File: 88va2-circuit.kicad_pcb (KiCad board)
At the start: 2 copper layers, 380 x 237.5 mm, 31 parts, among them CN2 FDD, CN4 TEXT BUS, CN5 LED, IC20 7407, IC21 uPD4990AC, IC22 DIP-14_W7.62mm, IC65 D65101GD110, X2 32.768K

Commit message: add internal layers (GND and power)
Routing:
- net GND: track 139.7 -> 1252.1 mm, vias 4 -> 10
- net +5V: track 5.94 -> 735.6 mm
- net (no net): track 1731.3 -> 1751.0 mm
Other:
- copper layers 2 -> 4

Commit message: fix IC65
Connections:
- IC65 pad 1: unconnected-(IC65-VDD-Pad1) -> +5V
- IC65 pad 40: unconnected-(IC65-VDD-Pad40) -> +5V
- IC65 pad 74: unconnected-(IC65-CLC2-Pad74) -> C2
- IC65 pad 75: unconnected-(IC65-CLC1-Pad75) -> C1
- IC65 pad 76: unconnected-(IC65-CLC0-Pad76) -> C0
- IC65 pad 77: unconnected-(IC65-CLSTB-Pad77) -> CSTB
- IC65 pad 78: unconnected-(IC65-CLDO-Pad78) -> CDO
- IC65 pad 82: unconnected-(IC65-CLCLK-Pad82) -> CCLK
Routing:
- net +5V: track 735.6 -> 826.3 mm, vias 0 -> 2

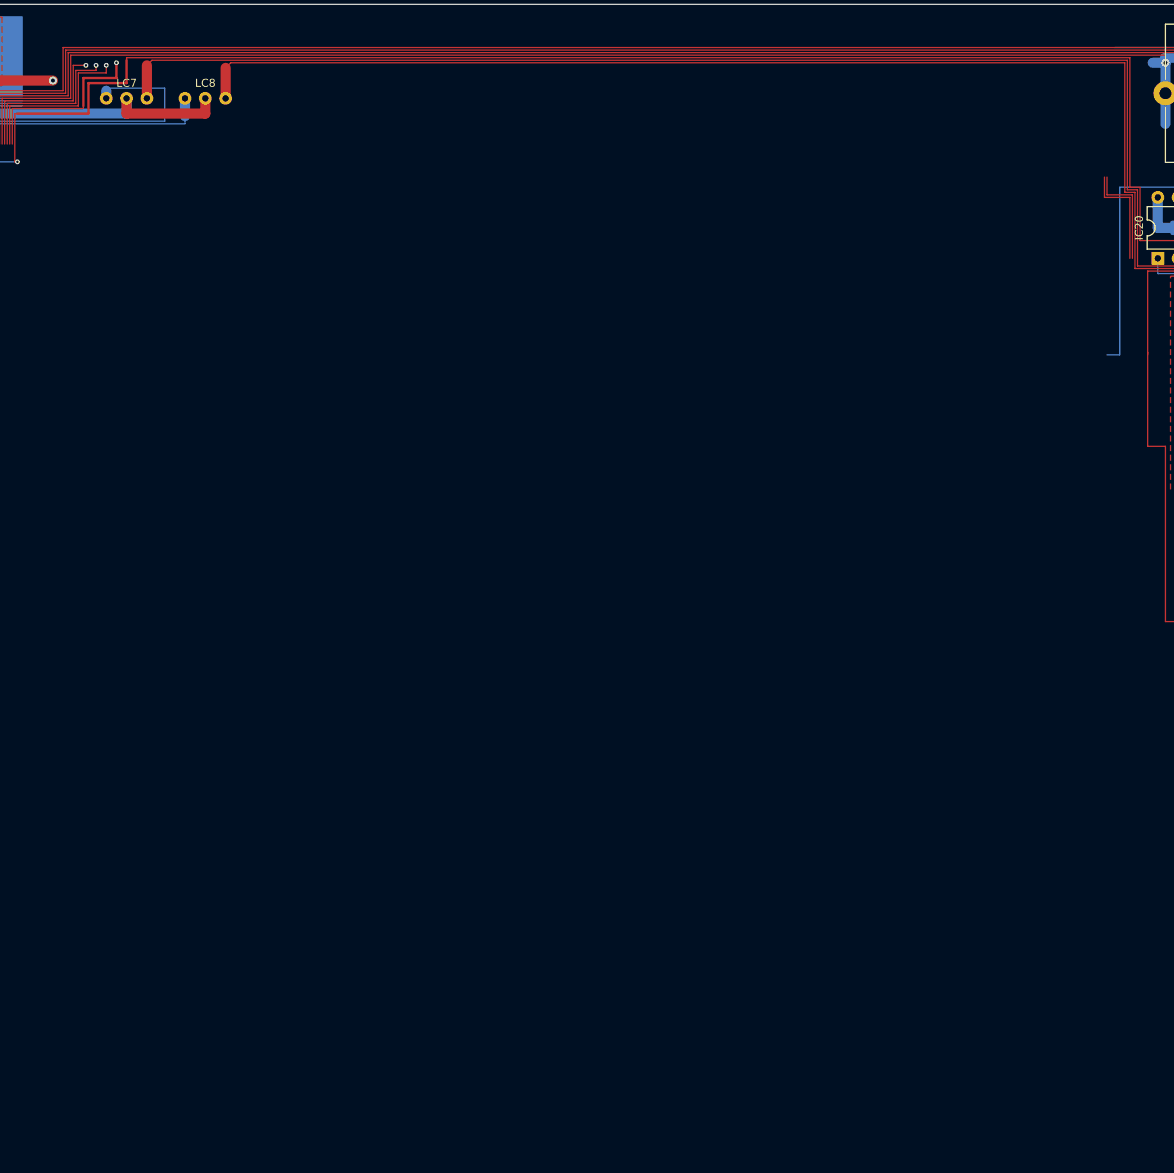
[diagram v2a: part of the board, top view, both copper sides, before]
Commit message: add IC13, MR6, IC9, IC1 footprints
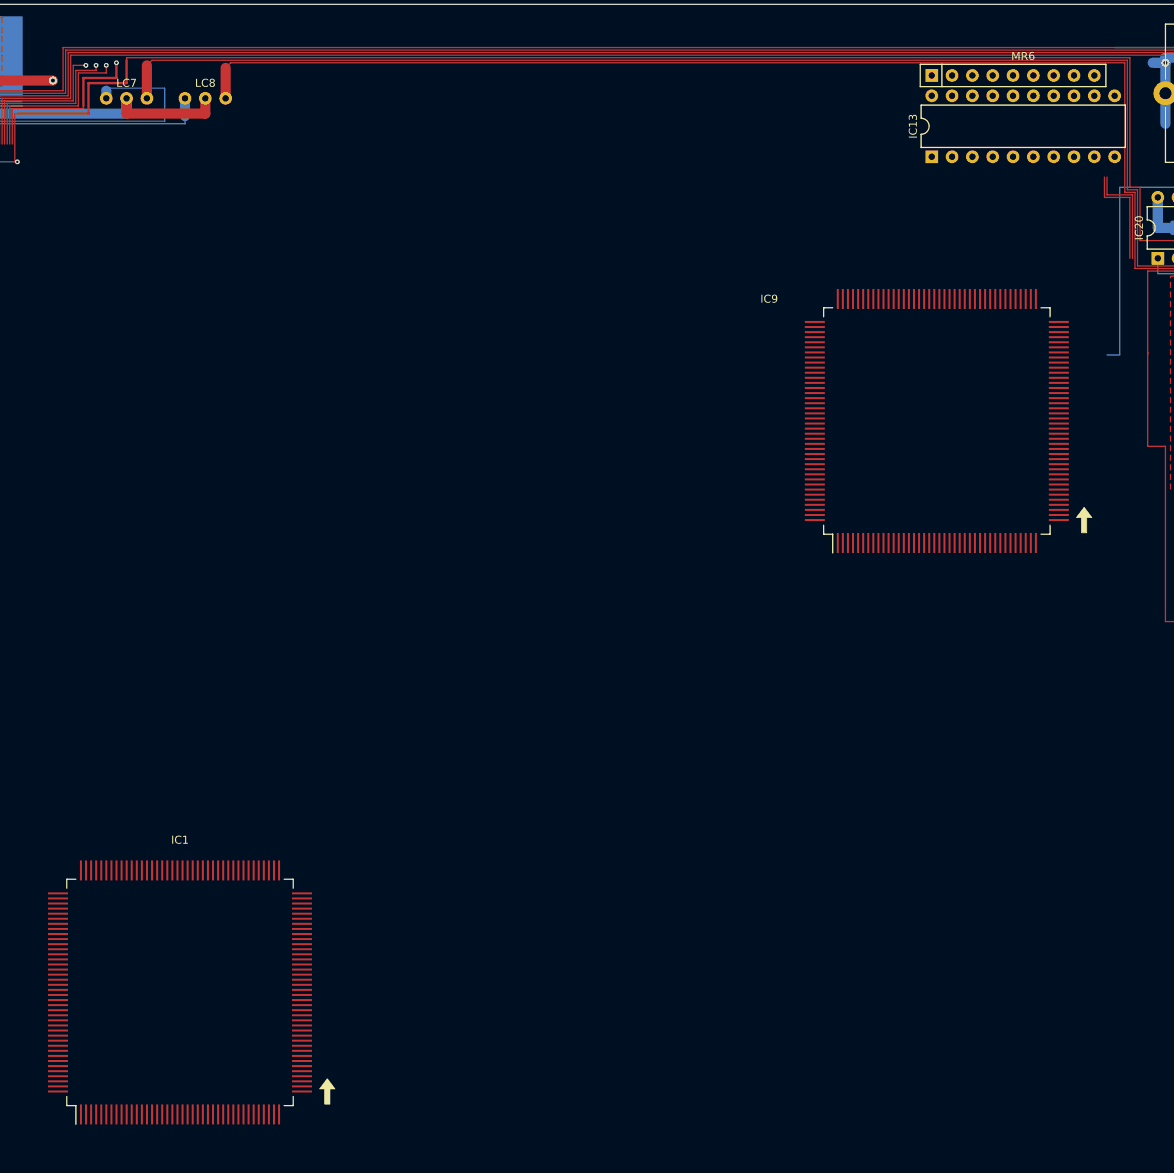
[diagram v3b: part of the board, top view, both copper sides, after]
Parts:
- added IC1: D65101GD055, 88va_Library:QFP-160_28x28_Pitch0.635mm, F.Cu at (45.4, 140.0)
- added IC13: SN74ALS374N, Package_DIP:DIP-20_W7.62mm, F.Cu at (139.3, 35.5)
- added IC9: D65200GD076, 88va_Library:QFP-160_28x28_Pitch0.635mm, F.Cu at (140.0, 68.6)
- added MR6: 33kΩ, Resistor_THT:R_Array_SIP9, F.Cu at (139.3, 25.4)

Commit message: wire IC13
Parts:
- added C60: C_Small, Capacitor_SMD:C_1206_3216Metric, B.Cu at (158.2, 31.7)
- moved IC9 0.46 mm to (139.6, 68.3)
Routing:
- net (no net): track 1751.0 -> 2510.1 mm, vias 29 -> 58
- net GCS0: track 0.00 -> 84.8 mm, vias 0 -> 2
- net Net-(IC13-7D): track 0.00 -> 70.5 mm, vias 0 -> 1
- net Net-(IC13-2D): track 0.00 -> 68.9 mm, vias 0 -> 2
- net Net-(IC13-6D): track 0.00 -> 65.1 mm, vias 0 -> 1
- net Net-(IC13-1D): track 0.00 -> 63.8 mm
- net Net-(IC13-5D): track 0.00 -> 55.9 mm
- net GCS1: track 0.00 -> 54.9 mm, vias 0 -> 1
- net Net-(IC13-3D): track 0.00 -> 54.9 mm
- net Net-(IC13-4D): track 0.00 -> 53.7 mm
- net Net-(IC13-CLK): track 0.00 -> 36.2 mm
- net +5V: track 826.3 -> 862.1 mm, vias 2 -> 4
- net Net-(IC13-8D): track 0.00 -> 12.1 mm
- net GND: track 1252.1 -> 1258.4 mm
- net GCS2: track 0.00 -> 2.54 mm

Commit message: wire IC13
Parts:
- added R18: ??, Resistor_SMD:R_1206_3216Metric, B.Cu at (96.3, 24.1)
- added REF**: DIP-20_W7.62mm, Package_DIP:DIP-20_W7.62mm, F.Cu at (111.4, 35.5)
- moved LC6 0.95 mm to (20.3, 40.6)
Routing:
- net ILCLK1: track 0.00 -> 323.8 mm, vias 0 -> 2
- net GCS2: track 2.54 -> 313.0 mm, vias 0 -> 1
- net GCS3: track 0.00 -> 304.8 mm, vias 0 -> 2
- net ILCLK0: track 0.00 -> 303.8 mm, vias 0 -> 2
- net GCS1: track 54.9 -> 345.1 mm, vias 1 -> 3
- net DTM0: track 0.00 -> 285.7 mm, vias 0 -> 2
- net GCS0: track 84.8 -> 356.5 mm, vias 2 -> 3
- net Net-(IC13-OE): track 0.00 -> 96.4 mm, vias 0 -> 3
- net (no net): track 2510.1 -> 2450.4 mm, vias 58 -> 60
- net Net-(IC13-8D): track 12.1 -> 54.2 mm
- net Net-(IC13-5D): track 55.9 -> 67.0 mm
- net +5V: track 862.1 -> 853.6 mm, vias 4 -> 3
- net Net-(IC13-6D): track 65.1 -> 72.1 mm
- net Net-(IC13-3D): track 54.9 -> 61.3 mm
- net Net-(IC13-7D): track 70.5 -> 76.5 mm
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
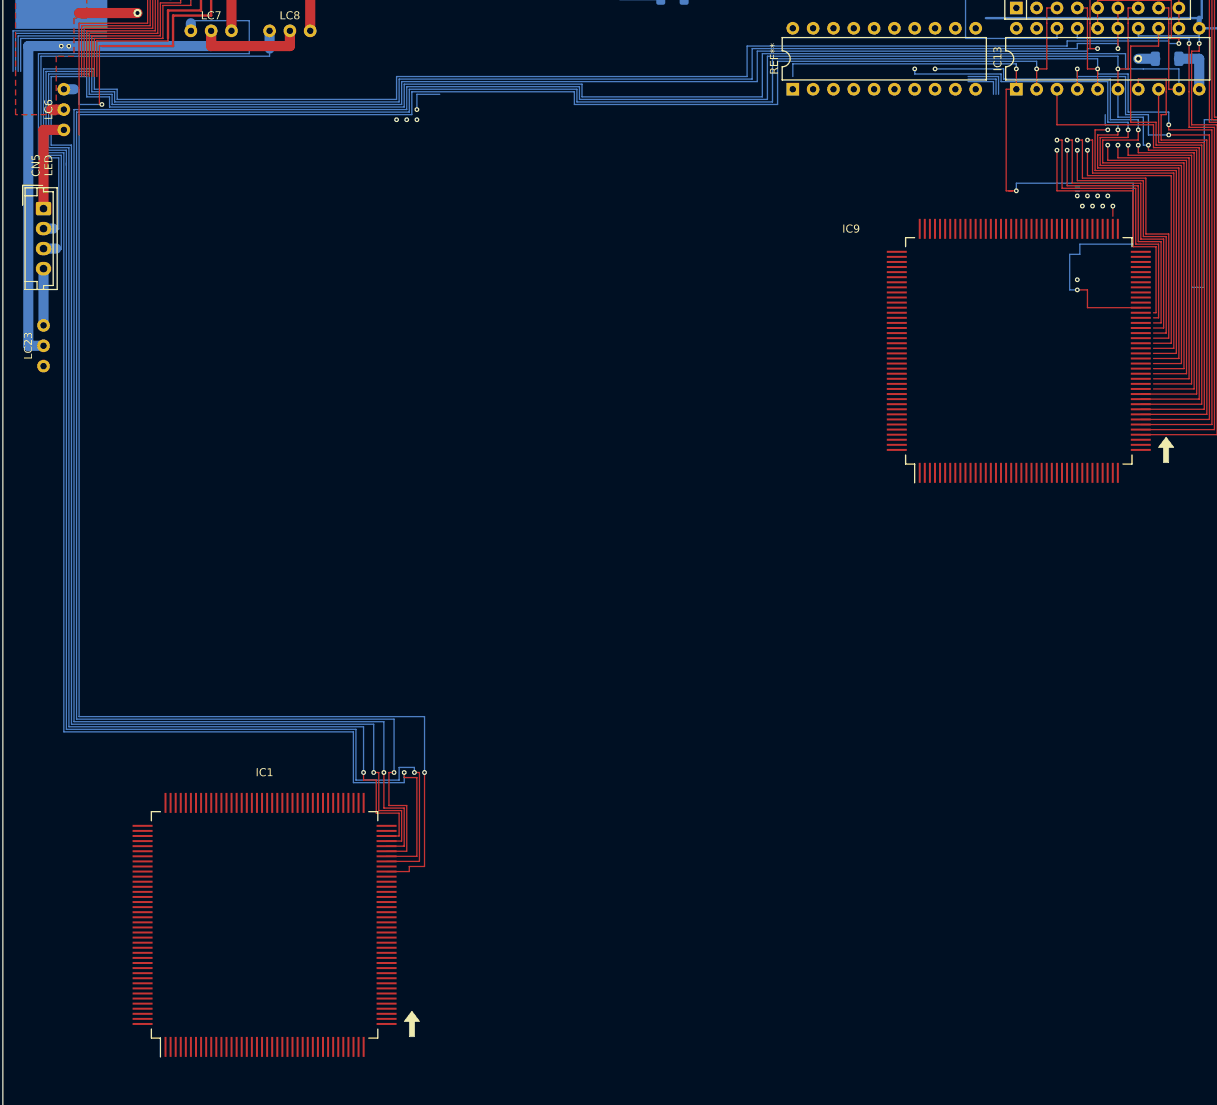
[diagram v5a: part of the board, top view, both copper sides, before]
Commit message: fix pitch of IC1 pads
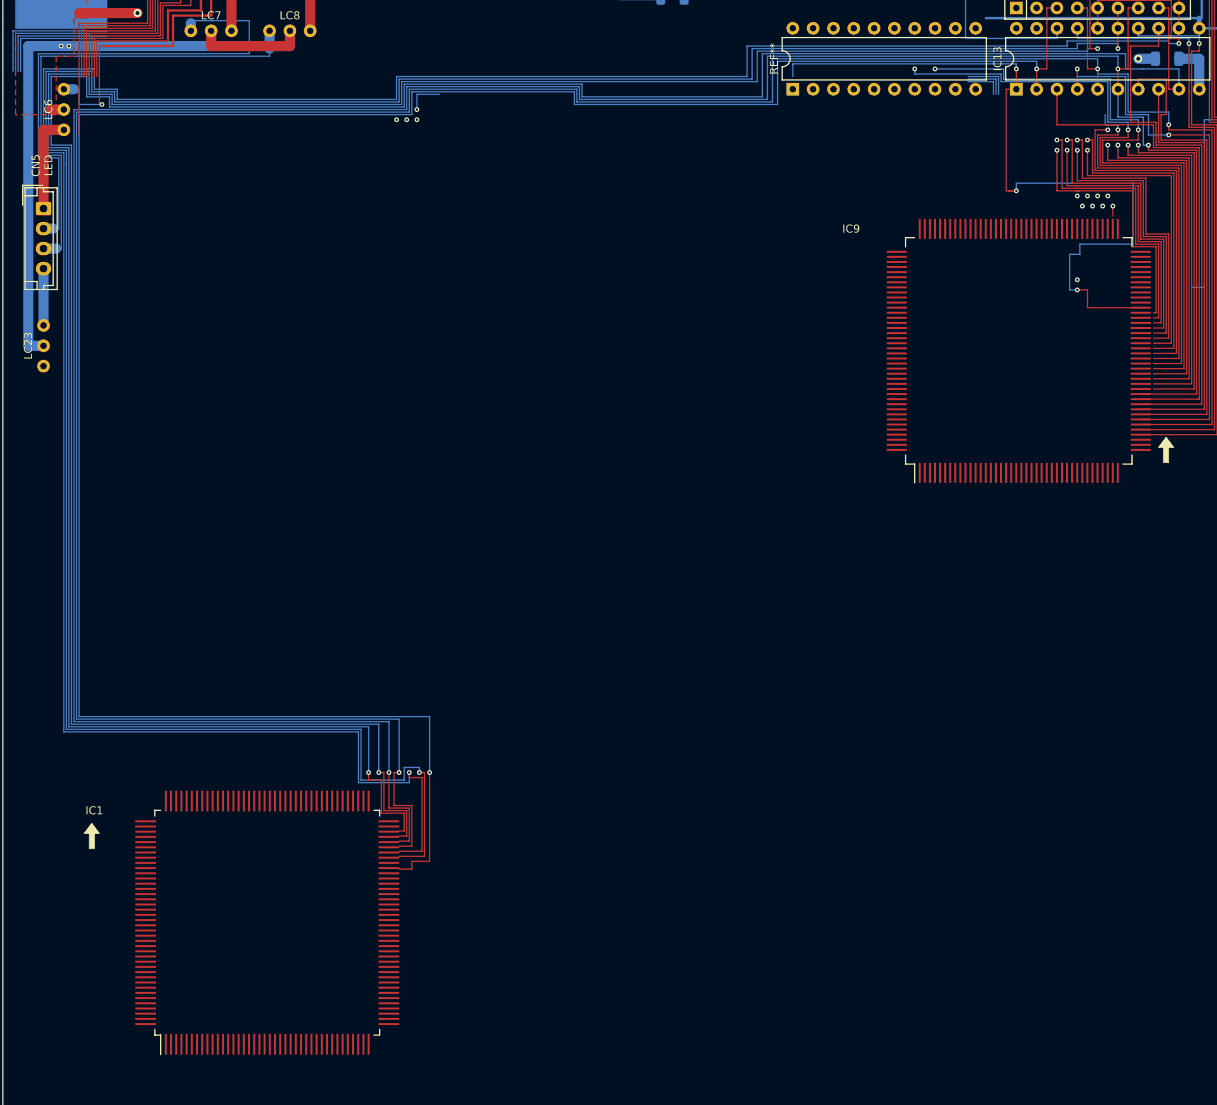
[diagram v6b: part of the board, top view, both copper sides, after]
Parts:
- added REF**: GAL_mark, 88va_Library:GAL_mark, F.Cu at (23.8, 127.3)
- IC1: footprint 88va_Library:QFP-160_28x28_Pitch0.635mm -> 88va_Library:QFP-160_27.8x27.8_Pitch0.65mm
- moved IC1 0.43 mm to (45.7, 139.7)
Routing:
- net GCS0: track 356.5 -> 355.6 mm
- net ILCLK1: track 323.8 -> 322.9 mm
- net ILCLK0: track 303.8 -> 302.9 mm
- net GCS2: track 313.0 -> 312.1 mm
- net GCS3: track 304.8 -> 303.8 mm
- net GCS1: track 345.1 -> 344.2 mm
- net DTM0: track 285.7 -> 285.1 mm

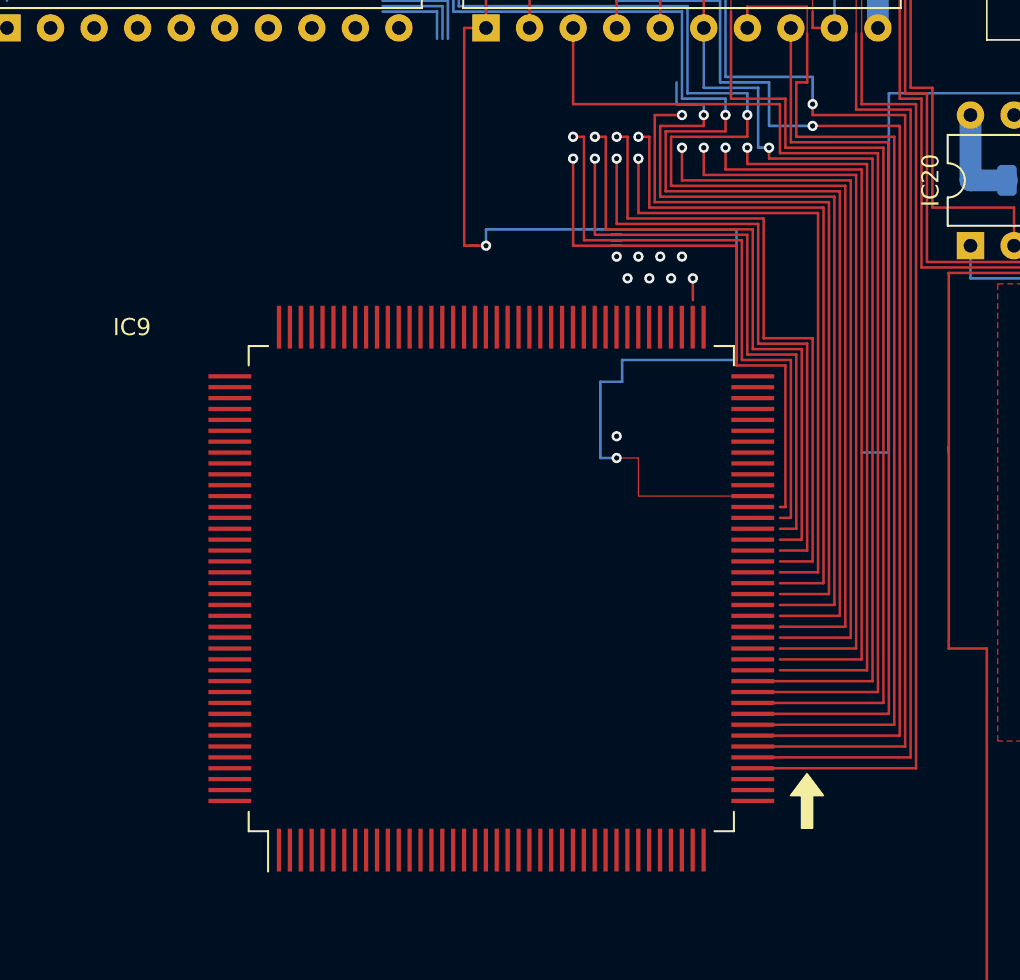
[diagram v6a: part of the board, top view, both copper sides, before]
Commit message: fix pitch of IC9 pads
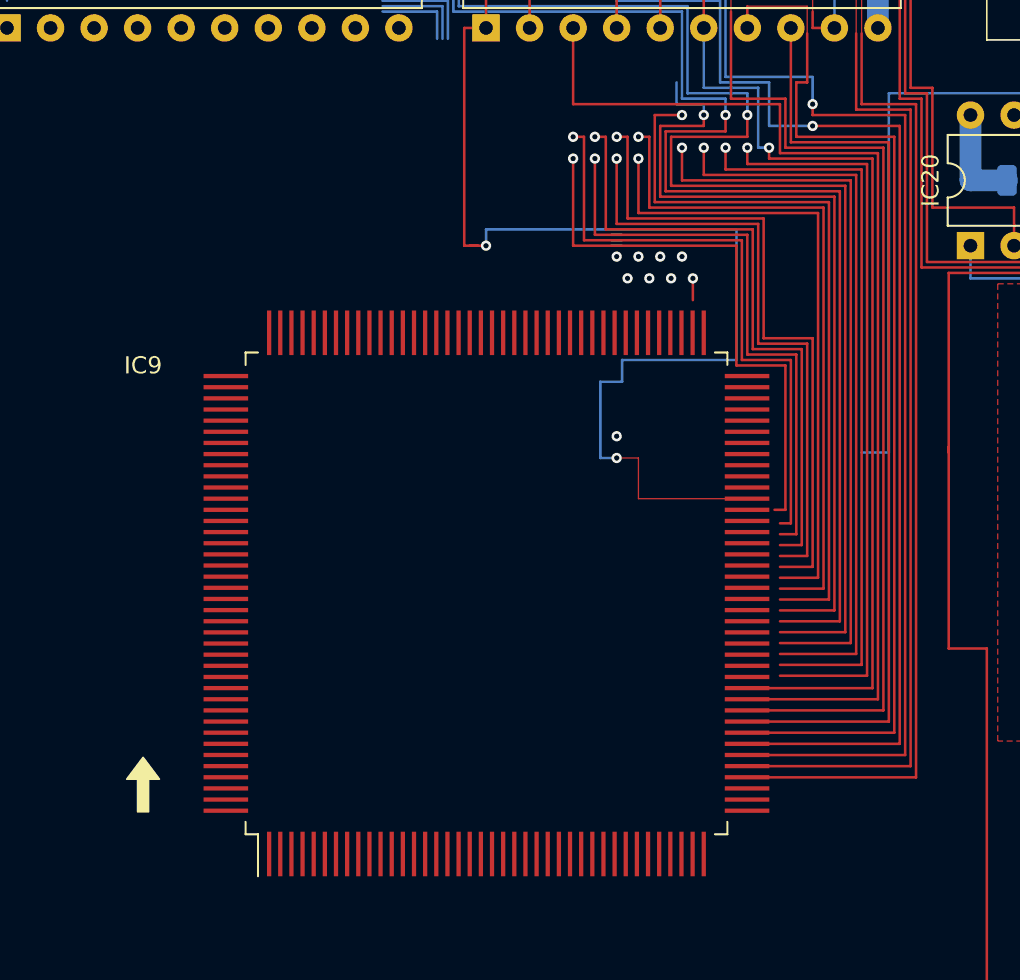
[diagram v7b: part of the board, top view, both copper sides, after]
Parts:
- added REF**: GAL_mark, 88va_Library:GAL_mark, F.Cu at (119.3, 78.1)
- IC9: footprint 88va_Library:QFP-160_28x28_Pitch0.635mm -> 88va_Library:QFP-160_27.8x27.8_Pitch0.65mm
- moved IC9 0.40 mm to (139.4, 68.5)
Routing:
- net (no net): track 2450.4 -> 2455.7 mm
- net Net-(IC13-6D): track 72.1 -> 72.9 mm
- net Net-(IC13-7D): track 76.5 -> 77.4 mm
- net GCS0: track 355.6 -> 356.4 mm
- net Net-(IC13-2D): track 71.4 -> 72.2 mm
- net Net-(IC13-3D): track 61.3 -> 62.1 mm
- net Net-(IC13-4D): track 53.7 -> 54.4 mm
- net Net-(IC13-5D): track 67.0 -> 67.8 mm
- net Net-(IC13-1D): track 63.8 -> 64.6 mm
- net GCS1: track 344.2 -> 344.9 mm
